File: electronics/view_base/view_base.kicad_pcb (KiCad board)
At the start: 2 copper layers, 81.2 x 81.2 mm, 107 parts, among them J1 BLDC, J2 USB_C_Receptacle_USB2.0, J3 LCD, J4 A, J5 B, Q1 MMBT4403, Q2 UMH3N, U1 MT6701-CT, U2 T-Micro32_Plus, U3 CH340C, U4 HX711, U5 TMC6300, U6 AP2114HA-3.3, U7 SN74LV1T34DBV, U8 VEML7700, U9 TS1117BCW33_RPG

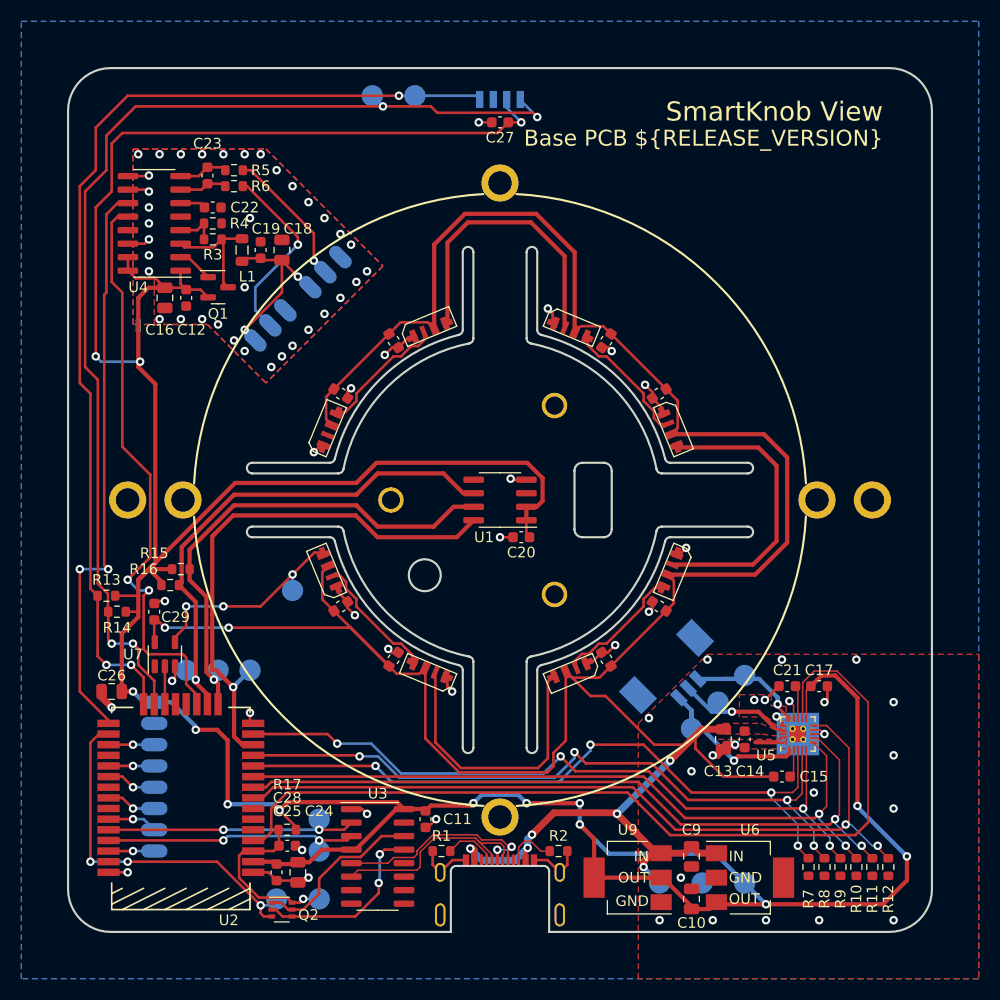
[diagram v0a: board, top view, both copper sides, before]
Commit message: Mod v1
- ESP32-S3-MINI-1N8
- 24x WS2812 20x20 LED
- SMD Resistors 4 direction Force Sensor
- Accelerometer
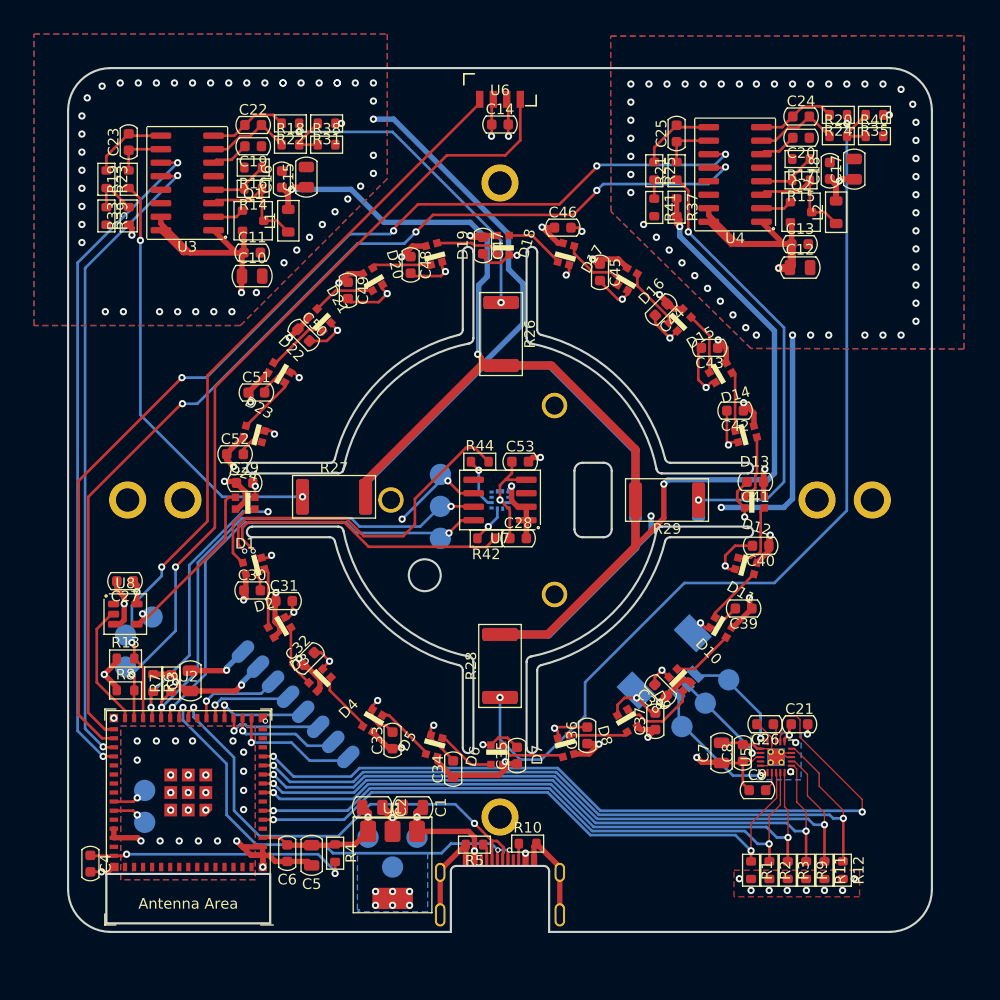
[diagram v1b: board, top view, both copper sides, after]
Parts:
- removed J4: A, SolderPads:SolderPads_2mm_3_STRAIN
- removed J5: B, SolderPads:SolderPads_2mm_3_STRAIN
- removed NT1: NetTie_2, NetTie:NetTie-2_SMD_Pad0.5mm
- removed TP15: TX, Modified:TestPoint_Pad_D2.0mm_ValueSilk
- removed TP16: RX, Modified:TestPoint_Pad_D2.0mm_ValueSilk
- removed U9: TS1117BCW33_RPG, Modified:SOT-223-3_TabPin2_GndOutIn
- removed Z10: BLDCMotor, BOM_Only:bom_only_no_pin
- removed Z7, Z8: RotorScrew (BOM-only), BOM_Only:bom_only_no_pin
- removed Z9: WatchGlass39.5mm, BOM_Only:bom_only_no_pin
- added C30: 0.1uF, Capacitor_SMD_AKL:C_0603_1608Metric, F.Cu at (76.7, 108.5)
- added C31: 0.1uF, Capacitor_SMD_AKL:C_0603_1608Metric, F.Cu at (79.7, 109.5)
- added C32: 0.1uF, Capacitor_SMD_AKL:C_0603_1608Metric, F.Cu at (82.0, 114.9)
- added C33: 0.1uF, Capacitor_SMD_AKL:C_0603_1608Metric, F.Cu at (89.9, 122.6)
- added C34: 0.1uF, Capacitor_SMD_AKL:C_0603_1608Metric, F.Cu at (95.6, 125.3)
- added C35: 0.1uF, Capacitor_SMD_AKL:C_0603_1608Metric, F.Cu at (101.6, 124.0)
- added C36: 0.1uF, Capacitor_SMD_AKL:C_0603_1608Metric, F.Cu at (108.2, 122.1)
- added C37: 0.1uF, Capacitor_SMD_AKL:C_0603_1608Metric, F.Cu at (114.6, 120.8)
- added C38: 0.1uF, Capacitor_SMD_AKL:C_0603_1608Metric, F.Cu at (115.1, 117.9)
- added C39: 0.1uF, Capacitor_SMD_AKL:C_0603_1608Metric, F.Cu at (122.9, 110.2)
- added C40: 0.1uF, Capacitor_SMD_AKL:C_0603_1608Metric, F.Cu at (124.5, 104.3)
- added C41: 0.1uF, Capacitor_SMD_AKL:C_0603_1608Metric, F.Cu at (124.0, 98.3)
- added C42: 0.1uF, Capacitor_SMD_AKL:C_0603_1608Metric, F.Cu at (122.1, 91.6)
- added C43: 0.1uF, Capacitor_SMD_AKL:C_0603_1608Metric, F.Cu at (119.7, 85.7)
- added C44: 0.1uF, Capacitor_SMD_AKL:C_0603_1608Metric, F.Cu at (115.2, 82.1)
- added C45: 0.1uF, Capacitor_SMD_AKL:C_0603_1608Metric, F.Cu at (109.4, 78.6)
- added C46: 0.1uF, Capacitor_SMD_AKL:C_0603_1608Metric, F.Cu at (105.9, 74.4)
- added C47: 0.1uF, Capacitor_SMD_AKL:C_0603_1608Metric, F.Cu at (98.4, 76.1)
- added C48: 0.1uF, Capacitor_SMD_AKL:C_0603_1608Metric, F.Cu at (91.6, 77.9)
- added C49: 0.1uF, Capacitor_SMD_AKL:C_0603_1608Metric, F.Cu at (85.7, 80.3)
- added C50: 0.1uF, Capacitor_SMD_AKL:C_0603_1608Metric, F.Cu at (81.5, 84.5)
- added C51: 0.1uF, Capacitor_SMD_AKL:C_0603_1608Metric, F.Cu at (77.1, 89.9)
- added C52: 0.1uF, Capacitor_SMD_AKL:C_0603_1608Metric, F.Cu at (75.1, 95.7)
- added C53: 1uF, Capacitor_SMD_AKL:C_0603_1608Metric, F.Cu at (101.9, 96.4)
- added D10: WS2812-2020, CrumpPrints:WS2812-2020, F.Cu at (116.9, 116.9)
- added D11: WS2812-2020, CrumpPrints:WS2812-2020, F.Cu at (120.8, 112.0)
- added D12: WS2812-2020, CrumpPrints:WS2812-2020, F.Cu at (123.1, 106.2)
- added D13: WS2812-2020, CrumpPrints:WS2812-2020, F.Cu at (123.9, 100.2)
- added D14: WS2812-2020, CrumpPrints:WS2812-2020, F.Cu at (123.1, 93.8)
- added D15: WS2812-2020, CrumpPrints:WS2812-2020, F.Cu at (120.8, 88.0)
- added D16: WS2812-2020, CrumpPrints:WS2812-2020, F.Cu at (116.9, 83.1)
- added D17: WS2812-2020, CrumpPrints:WS2812-2020, F.Cu at (112.0, 79.2)
- added D18: WS2812-2020, CrumpPrints:WS2812-2020, F.Cu at (106.2, 76.9)
- added D19: WS2812-2020, CrumpPrints:WS2812-2020, F.Cu at (100.3, 76.0)
- added D20: WS2812-2020, CrumpPrints:WS2812-2020, F.Cu at (93.8, 76.9)
- added D21: WS2812-2020, CrumpPrints:WS2812-2020, F.Cu at (88.0, 79.2)
- added D22: WS2812-2020, CrumpPrints:WS2812-2020, F.Cu at (83.1, 83.1)
- added D23: WS2812-2020, CrumpPrints:WS2812-2020, F.Cu at (79.2, 88.0)
- added D24: WS2812-2020, CrumpPrints:WS2812-2020, F.Cu at (76.9, 93.8)
- added D9: WS2812-2020, CrumpPrints:WS2812-2020, F.Cu at (112.0, 120.8)
- added IC1: MXC6655XA, KiCad:MXC6655XA, B.Cu at (100.0, 100.0)
- added L2: 3.3uH, Inductor_SMD_AKL:L_0805_2012Metric, F.Cu at (131.6, 72.9)
- added R18: 100, Resistor_SMD_AKL:R_0603_1608Metric, F.Cu at (80.3, 66.6)
- added R19: 100, Resistor_SMD_AKL:R_0603_1608Metric, F.Cu at (65.1, 69.8)
- added R20: 100, Resistor_SMD_AKL:R_0603_1608Metric, F.Cu at (131.8, 65.8)
- added R21: 100, Resistor_SMD_AKL:R_0603_1608Metric, F.Cu at (116.6, 69.0)
- added R22: 100, Resistor_SMD_AKL:R_0603_1608Metric, F.Cu at (80.3, 64.6)
- added R23: 100, Resistor_SMD_AKL:R_0603_1608Metric, F.Cu at (63.0, 69.8)
- added R24: 100, Resistor_SMD_AKL:R_0603_1608Metric, F.Cu at (131.8, 63.8)
- added R25: 100, Resistor_SMD_AKL:R_0603_1608Metric, F.Cu at (114.5, 69.0)
- added R26: 1K, Resistor_SMD_AKL:R_2512_6332Metric, F.Cu at (100.1, 84.4)
- added R27: 1K, Resistor_SMD_AKL:R_2512_6332Metric, F.Cu at (84.4, 99.7)
- added R28: 1K, Resistor_SMD_AKL:R_2512_6332Metric, F.Cu at (100.0, 115.6)
- added R29: 1K, Resistor_SMD_AKL:R_2512_6332Metric, F.Cu at (115.7, 100.0)
- added R30: 1K, Resistor_SMD_AKL:R_2512_6332Metric, B.Cu at (100.1, 84.4)
- added R31: 1k, Resistor_SMD_AKL:R_0603_1608Metric, F.Cu at (83.7, 64.6)
- added R32: 1K, Resistor_SMD_AKL:R_2512_6332Metric, B.Cu at (84.4, 99.7)
- added R33: 1k, Resistor_SMD_AKL:R_0603_1608Metric, F.Cu at (65.1, 73.3)
- added R34: 1K, Resistor_SMD_AKL:R_2512_6332Metric, B.Cu at (100.0, 115.6)
- added R35: 1k, Resistor_SMD_AKL:R_0603_1608Metric, F.Cu at (135.2, 63.8)
- added R36: 1K, Resistor_SMD_AKL:R_2512_6332Metric, B.Cu at (115.7, 100.3)
- added R37: 1k, Resistor_SMD_AKL:R_0603_1608Metric, F.Cu at (116.6, 72.5)
- added R38: 1k, Resistor_SMD_AKL:R_0603_1608Metric, F.Cu at (83.7, 66.6)
- added R39: 1k, Resistor_SMD_AKL:R_0603_1608Metric, F.Cu at (63.0, 73.3)
- added R40: 1k, Resistor_SMD_AKL:R_0603_1608Metric, F.Cu at (135.2, 65.8)
- added R41: 1k, Resistor_SMD_AKL:R_0603_1608Metric, F.Cu at (114.5, 72.5)
- added R42: 2.7k, Resistor_SMD_AKL:R_0603_1608Metric, F.Cu at (98.7, 103.6)
- added R44: 2.7k, Resistor_SMD_AKL:R_0603_1608Metric, F.Cu at (98.1, 96.4)
- C1, C12, C15, C17, C2, C3, C5: value 0.1uF -> 10uF; footprint Capacitor_SMD:C_0603_1608Metric -> Capacitor_SMD_AKL:C_0805_2012Metric
- C10: footprint Capacitor_SMD:C_0805_2012Metric -> Capacitor_SMD_AKL:C_0805_2012Metric
- C11, C14, C19, C20, C21, C22, C23, C25, C27, C29, C6, C8: footprint Capacitor_SMD:C_0603_1608Metric -> Capacitor_SMD_AKL:C_0603_1608Metric
- C13: value 22uF -> 0.1uF; footprint Capacitor_SMD:C_0805_2012Metric -> Capacitor_SMD_AKL:C_0603_1608Metric
- C16, C18, C24, C26, C9: value 10uF -> 0.1uF; footprint Capacitor_SMD:C_0805_2012Metric -> Capacitor_SMD_AKL:C_0603_1608Metric
- C28: value 1uF -> 0.1uF; footprint Capacitor_SMD:C_0603_1608Metric -> Capacitor_SMD_AKL:C_0603_1608Metric
- C4: value 0.1uF -> 1uF; footprint Capacitor_SMD:C_0603_1608Metric -> Capacitor_SMD_AKL:C_0603_1608Metric
- C7: value 0.1uF -> 22uF; footprint Capacitor_SMD:C_0603_1608Metric -> Capacitor_SMD_AKL:C_0805_2012Metric
- D1, D2, D3, D4, D5, D6, D7, D8: value SK6812SIDE-A -> WS2812-2020; footprint sk6812:SK6812-SIDE-A -> CrumpPrints:WS2812-2020
- J1: value BLDC -> LCD; footprint Molex:532610371 -> SolderPads:SolderPads_2mm_8
- J3: value LCD -> BLDC; footprint SolderPads:SolderPads_2mm_8 -> Molex:532610371
- L1: footprint Inductor_SMD:L_0805_2012Metric -> Inductor_SMD_AKL:L_0805_2012Metric
- Q1: footprint Package_TO_SOT_SMD:SOT-23 -> Package_TO_SOT_SMD_AKL:SOT-23
- Q2: value UMH3N -> MMBT4403; footprint Package_TO_SOT_SMD:SOT-363_SC-70-6 -> Package_TO_SOT_SMD_AKL:SOT-23
- R1, R2: value 5.1k -> 10k; footprint Resistor_SMD:R_0603_1608Metric -> Resistor_SMD_AKL:R_0603_1608Metric
- R10: value 10k -> 5.1k; footprint Resistor_SMD:R_0603_1608Metric -> Resistor_SMD_AKL:R_0603_1608Metric
- R11, R12, R13, R3, R9: footprint Resistor_SMD:R_0603_1608Metric -> Resistor_SMD_AKL:R_0603_1608Metric
- R14, R15: value 2.2k -> 10k; footprint Resistor_SMD:R_0603_1608Metric -> Resistor_SMD_AKL:R_0603_1608Metric
- R16: value 2.2k -> 8.2k; footprint Resistor_SMD:R_0603_1608Metric -> Resistor_SMD_AKL:R_0603_1608Metric
- R17: value 10k -> 8.2k; footprint Resistor_SMD:R_0603_1608Metric -> Resistor_SMD_AKL:R_0603_1608Metric
- R4: value 8.2k -> 10k; footprint Resistor_SMD:R_0603_1608Metric -> Resistor_SMD_AKL:R_0603_1608Metric
- R5: value 100 -> 5.1k; footprint Resistor_SMD:R_0603_1608Metric -> Resistor_SMD_AKL:R_0603_1608Metric
- R6: value 100 -> 2.2k; footprint Resistor_SMD:R_0603_1608Metric -> Resistor_SMD_AKL:R_0603_1608Metric
- R7, R8: value 10k -> 2.2k; footprint Resistor_SMD:R_0603_1608Metric -> Resistor_SMD_AKL:R_0603_1608Metric
- TP10: value CLK -> W
- TP11: value DO -> LED
- TP12: value LED -> CSN
- TP13: value EN -> CLK
- TP14: value BOOT -> DO
- TP3: value GND -> TX
- TP4: value SDA -> RX
- TP5: value SCL -> GND
- TP6: value U -> SDA
- TP7: value V -> SCL
- TP8: value W -> U
- TP9: value CSN -> V
- U1: value MT6701-CT -> AP2114HA-3.3; footprint Package_SO:SOIC-8_3.9x4.9mm_P1.27mm -> Package_TO_SOT_SMD_AKL:SOT-223-3_TabPin2
- U2: value T-Micro32_Plus -> ESP32-S3-MINI-1; footprint lilygo_micro32:T-Micro32 -> Espressif:ESP32-S3-MINI-1
- U3: value CH340C -> HX711; footprint Package_SO:SOIC-16_3.9x9.9mm_P1.27mm -> Package_SO_AKL:SOIC-16_3.9x9.9mm_P1.27mm
- U4: footprint Package_SO:SOIC-16_3.9x9.9mm_P1.27mm -> Package_SO_AKL:SOIC-16_3.9x9.9mm_P1.27mm
- U6: value AP2114HA-3.3 -> VEML7700; footprint Modified:SOT-223-3_TabPin2_InGndOut -> VEML7700:VEML7700-TOP
- U7: value SN74LV1T34DBV -> MT6701-CT; footprint Package_TO_SOT_SMD:SOT-23-5 -> Package_SO_AKL:SOIC-8_3.9x4.9mm_P1.27mm
- U8: value VEML7700 -> SN74LV1T34DBV; footprint VEML7700:VEML7700-TOP -> Package_TO_SOT_SMD_AKL:SOT-23-5; moved to F.Cu
- Z1, Z2, Z3: value BF350-3AA Strain Gauge -> RotorScrew (BOM-only); footprint strain:BF350-3AA -> BOM_Only:bom_only_no_pin; moved to F.Cu
- Z4: value BF350-3AA Strain Gauge -> WatchGlass39.5mm; footprint strain:BF350-3AA -> BOM_Only:bom_only_no_pin; moved to F.Cu
- Z5: value dummy_keepouts -> BLDCMotor; footprint view_custom:ViewKeepouts3d -> BOM_Only:bom_only_no_pin
- Z6: value RotorScrew (BOM-only) -> dummy_keepouts; footprint BOM_Only:bom_only_no_pin -> view_custom:ViewKeepouts3d
- moved Z4 105.9 mm to (177.0, 65.7), turned to 0 degrees
- moved Z3 96.7 mm to (177.4, 73.4), turned to 0 degrees
- moved C24 85.4 mm to (128.3, 63.9), turned to 0 degrees
- moved Z5 83.5 mm to (177.2, 68.1)
- moved Q2 81.7 mm to (128.3, 72.9)
- moved R3 80.2 mm to (127.0, 134.8), turned to -90 degrees
- moved R17 79.4 mm to (128.3, 68.0)
- moved C25 79.0 mm to (116.6, 65.5), turned to 90 degrees
- moved U6 78.1 mm to (100.0, 61.0)
- moved TP4 72.9 mm to (66.6, 130.3), turned to 180 degrees
- moved TP5 72.5 mm to (89.9, 134.5), turned to 90 degrees
- moved C15 71.9 mm to (81.8, 69.6), turned to 90 degrees
- moved C10 71.7 mm to (76.7, 78.9), turned to 0 degrees
- moved R15 70.5 mm to (128.3, 69.9), turned to 180 degrees
- moved Z1 68.1 mm to (177.1, 70.8), turned to 0 degrees
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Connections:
- C12 pad 2: GNDA -> GND
- C13 pad 1: +5V -> +3V3
- C14 pad 1: +5V -> +3V3
- C15 pad 1: +5V -> /AVDD
- C15 pad 2: Net-(C15-Pad2) -> GND
- C16 pad 1: +3V3 -> /AVDD
- C16 pad 2: GNDA -> GND
- C17 pad 1: +3V3 -> /AVDD
- C18 pad 1: /STRAIN_E+ -> /AVDD
- C18 pad 2: GNDA -> GND
- C19 pad 1: /STRAIN_E+ -> GND
- C19 pad 2: GNDA -> Net-(C19-Pad2)
- C2 pad 1: +5V -> +3V3
- C20 pad 1: +3V3 -> GND
- C20 pad 2: GND -> Net-(C20-Pad2)
- C21 pad 1: Net-(C21-Pad1) -> +3V3
- C22 pad 1: GNDA -> Net-(C22-Pad1)
- C24 pad 1: +3V3 -> Net-(C24-Pad1)
- C24 pad 2: GND -> Net-(C24-Pad2)
- C25 pad 1: +3V3 -> Net-(C25-Pad1)
- C25 pad 2: GND -> Net-(C25-Pad2)
- C26 pad 1: +3V3 -> Net-(C26-Pad1)
- C27 pad 1: +3V3 -> +5V
- C28 pad 1: /ESP32_EN -> GND
- C28 pad 2: GND -> +3V3
- C3 pad 1: +5V -> +3V3
- C4 pad 1: +5V -> /ESP32_EN
- C5 pad 1: +5V -> +3V3
- C6 pad 1: +5V -> +3V3
- C9 pad 2: GND -> Net-(C9-Pad2)
- D1 pad 1: /LED_DATA_5V -> Net-(D1-Pad1)
- D1 pad 2: +5V -> GND
- D1 pad 3: Net-(D1-Pad3) -> /LED_DATA_5V
- D1 pad 4: GND -> +5V
- D2 pad 1: Net-(D1-Pad3) -> Net-(D2-Pad1)
- D2 pad 2: +5V -> GND
- D2 pad 3: Net-(D2-Pad3) -> Net-(D1-Pad1)
- D2 pad 4: GND -> +5V
- D3 pad 1: Net-(D2-Pad3) -> Net-(D3-Pad1)
- D3 pad 2: +5V -> GND
- D3 pad 3: Net-(D3-Pad3) -> Net-(D2-Pad1)
- D3 pad 4: GND -> +5V
- D4 pad 1: Net-(D3-Pad3) -> Net-(D4-Pad1)
- D4 pad 2: +5V -> GND
- D4 pad 3: Net-(D4-Pad3) -> Net-(D3-Pad1)
- D4 pad 4: GND -> +5V
- D5 pad 1: Net-(D4-Pad3) -> Net-(D5-Pad1)
- D5 pad 2: +5V -> GND
- D5 pad 3: Net-(D5-Pad3) -> Net-(D4-Pad1)
- D5 pad 4: GND -> +5V
- D6 pad 1: Net-(D5-Pad3) -> Net-(D6-Pad1)
- D6 pad 2: +5V -> GND
- D6 pad 3: Net-(D6-Pad3) -> Net-(D5-Pad1)
- D6 pad 4: GND -> +5V
- D7 pad 1: Net-(D6-Pad3) -> Net-(D7-Pad1)
- D7 pad 2: +5V -> GND
- D7 pad 3: Net-(D7-Pad3) -> Net-(D6-Pad1)
- D7 pad 4: GND -> +5V
- D8 pad 1: Net-(D7-Pad3) -> Net-(D8-Pad1)
- D8 pad 2: +5V -> GND
- D8 pad 3: unconnected-(D8-Pad3) -> Net-(D7-Pad1)
- D8 pad 4: GND -> +5V
- J1 pad 1: Net-(J1-Pad1) -> GND
- J1 pad 2: Net-(J1-Pad2) -> +3V3
- J1 pad 3: Net-(J1-Pad3) -> /LCD_BL
- J3 pad 1: +3V3 -> Net-(J3-Pad1)
- J3 pad 2: GND -> Net-(J3-Pad2)
- J3 pad 3: /LCD_RST -> Net-(J3-Pad3)
- L1 pad 2: /STRAIN_E+ -> /AVDD
- Q2 pad 1: /RTS -> Net-(Q2-Pad1)
- Q2 pad 2: /DTR -> +3V3
- Q2 pad 3: /ESP32_BOOT -> Net-(L2-Pad1)
- R1 pad 1: /USB_CC1 -> /TMC_UH
- R10 pad 1: /TMC_UL -> /USB_CC2
- R13 pad 2: /SDA -> /SCL
- R14 pad 1: +3V3 -> Net-(L1-Pad1)
- R14 pad 2: /SCL -> Net-(R14-Pad2)
- R15 pad 1: +3V3 -> Net-(L2-Pad1)
- R15 pad 2: /MAG_DO -> Net-(R15-Pad2)
- R16 pad 1: /MAG_CLK -> Net-(R14-Pad2)
- R16 pad 2: +3V3 -> GND
- R17 pad 1: +3V3 -> Net-(R15-Pad2)
- R17 pad 2: /ESP32_EN -> GND
- R2 pad 1: /USB_CC2 -> /TMC_VH
- R3 pad 1: Net-(L1-Pad1) -> /TMC_WH
- R3 pad 2: Net-(R3-Pad2) -> GND
- R4 pad 1: Net-(R3-Pad2) -> +3V3
- R4 pad 2: GNDA -> /ESP32_EN
- R5 pad 1: Net-(C23-Pad2) -> /USB_CC1
- R5 pad 2: /STRAIN_S- -> GND
- R6 pad 1: /STRAIN_S+ -> +3V3
- R6 pad 2: Net-(C23-Pad1) -> /MAG_DO
- R7 pad 1: /TMC_UH -> /MAG_CLK
- R7 pad 2: GND -> +3V3
- R8 pad 1: /TMC_VH -> +3V3
- R8 pad 2: GND -> /SDA
- R9 pad 1: /TMC_WH -> /TMC_UL
- TP10 pad 1: /MAG_CLK -> Net-(J3-Pad1)
- TP11 pad 1: /MAG_DO -> /LED_DATA_5V
- TP12 pad 1: /LED_DATA_5V -> /MAG_CSN
- TP13 pad 1: /ESP32_EN -> /MAG_CLK
- TP14 pad 1: /ESP32_BOOT -> /MAG_DO
- TP3 pad 1: GND -> Net-(TP3-Pad1)
- TP4 pad 1: /SDA -> Net-(TP4-Pad1)
- TP5 pad 1: /SCL -> GND
- TP6 pad 1: Net-(J1-Pad3) -> /SDA
- TP7 pad 1: Net-(J1-Pad2) -> /SCL
- TP8 pad 1: Net-(J1-Pad1) -> Net-(J3-Pad3)
- TP9 pad 1: /MAG_CSN -> Net-(J3-Pad2)
- U1 pad 1: +3V3 -> +5V
- U1 pad 2: +3V3 -> GND
- U1 pad 3: unconnected-(U1-Pad3) -> +3V3
- U2 pad 10: /TMC_UL -> /TMC_WL
- U2 pad 11: /TMC_UH -> /TMC_VL
- U2 pad 12: /TMC_VH -> /TMC_DIAG
- U2 pad 13: /MAG_CSN -> unconnected-(U2-Pad13)
- U2 pad 14: /TMC_WH -> unconnected-(U2-Pad14)
- U2 pad 15: GND -> unconnected-(U2-Pad15)
- U2 pad 16: /MAG_CLK -> /LCD_RST
- U2 pad 17: /MAG_DO -> /LCD_DATA
- U2 pad 18: /STRAIN_DO -> /LCD_SCK
- U2 pad 19: unconnected-(U2-Pad19) -> /LCD_CS
- U2 pad 2: +3V3 -> GND
- U2 pad 20: unconnected-(U2-Pad20) -> /LCD_CMD
- U2 pad 21: /LED_DATA_3V3 -> /LCD_BL
- U2 pad 22: /SCL -> unconnected-(U2-Pad22)
- U2 pad 23: /SDA -> /USB_D-
- U2 pad 24: /STRAIN_SCK -> /USB_D+
- U2 pad 25: /ESP32_BOOT -> /MAG_CSN
- U2 pad 26: /LCD_RST -> /MAG_CLK
- U2 pad 27: unconnected-(U2-Pad27) -> /MAG_DO
- U2 pad 28: /LCD_SCK -> /SCL
- U2 pad 29: /LCD_DATA -> /SDA
- U2 pad 3: /ESP32_EN -> +3V3
- U2 pad 30: unconnected-(U2-Pad30) -> /LED_DATA
- U2 pad 31: /LCD_BACKLIGHT -> /STRAIN2_DO
- U2 pad 32: unconnected-(U2-Pad32) -> /STRAIN2_SCK
- U2 pad 33: /LCD_CS -> /STRAIN1_DO
- U2 pad 34: /USB_SERIAL_TXO -> /STRAIN1_SCK
- U2 pad 35: /USB_SERIAL_RXI -> unconnected-(U2-Pad35)
- U2 pad 36: /LCD_CMD -> unconnected-(U2-Pad36)
- U2 pad 38: GND -> unconnected-(U2-Pad38)
- U2 pad 4: /TMC_DIAG -> unconnected-(U2-Pad4)
- U2 pad 5: unconnected-(U2-Pad5) -> /TMC_UH
- U2 pad 6: unconnected-(U2-Pad6) -> /TMC_VH
- U2 pad 8: /TMC_VL -> /TMC_WH
- U2 pad 9: /TMC_WL -> /TMC_UL
- U3 pad 1: GND -> +3V3
- U3 pad 10: unconnected-(U3-Pad10) -> Net-(C23-Pad1)
- U3 pad 11: unconnected-(U3-Pad11) -> /STRAIN1_SCK
- U3 pad 12: unconnected-(U3-Pad12) -> /STRAIN1_DO
- U3 pad 13: /DTR -> unconnected-(U3-Pad13)
- U3 pad 14: /RTS -> GND
- U3 pad 15: unconnected-(U3-Pad15) -> +3V3
- U3 pad 2: /USB_SERIAL_TXO -> Net-(Q1-Pad1)
- U3 pad 3: /USB_SERIAL_RXI -> Net-(L1-Pad1)
- U3 pad 4: +3V3 -> Net-(R14-Pad2)
- U3 pad 5: /USB_D+ -> GND
- U3 pad 6: /USB_D- -> Net-(C19-Pad2)
- U3 pad 7: unconnected-(U3-Pad7) -> Net-(C22-Pad2)
- U3 pad 8: unconnected-(U3-Pad8) -> Net-(C22-Pad1)
- U3 pad 9: unconnected-(U3-Pad9) -> Net-(C23-Pad2)
- U4 pad 10: GNDA -> Net-(C25-Pad1)
- U4 pad 11: /STRAIN_SCK -> /STRAIN2_SCK
- U4 pad 12: /STRAIN_DO -> /STRAIN2_DO
- U4 pad 14: GNDA -> GND
- U4 pad 2: Net-(Q1-Pad1) -> Net-(Q2-Pad1)
- U4 pad 3: Net-(L1-Pad1) -> Net-(L2-Pad1)
- U4 pad 4: Net-(R3-Pad2) -> Net-(R15-Pad2)
- U4 pad 5: GNDA -> GND
- U4 pad 6: Net-(C22-Pad2) -> Net-(C20-Pad2)
- U4 pad 7: Net-(C23-Pad2) -> Net-(C24-Pad2)
- U4 pad 8: Net-(C23-Pad1) -> Net-(C24-Pad1)
- U4 pad 9: GNDA -> Net-(C25-Pad2)
- U5 pad 1: Net-(J1-Pad1) -> Net-(J3-Pad1)
- U5 pad 13: Net-(C21-Pad1) -> Net-(C26-Pad1)
- U5 pad 15: Net-(J1-Pad3) -> Net-(J3-Pad3)
- U5 pad 17: Net-(J1-Pad2) -> Net-(J3-Pad2)
- U5 pad 2: Net-(C15-Pad2) -> Net-(C9-Pad2)
- U6 pad 1: +5V -> /SCL
- U6 pad 2: GND -> +3V3
- U6 pad 3: +3V3 -> GND
- U7 pad 1: unconnected-(U7-Pad1) -> +3V3
- U7 pad 2: /LED_DATA_3V3 -> +3V3
- U7 pad 3: GND -> unconnected-(U7-Pad3)
- U7 pad 4: /LED_DATA_5V -> GND
- U7 pad 5: +5V -> unconnected-(U7-Pad5)
- U8 pad 1: /SCL -> unconnected-(U8-Pad1)
- U8 pad 2: +3V3 -> /LED_DATA
- U8 pad 4: /SDA -> /LED_DATA_5V
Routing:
- net GND: track 69.1 -> 300.2 mm, vias 47 -> 175
- net /AVDD: track 0.00 -> 213.2 mm, vias 0 -> 8
- net +5V: track 256.1 -> 459.7 mm, vias 8 -> 28
- net /STRAIN2_SCK: track 0.00 -> 101.5 mm, vias 0 -> 4
- net /STRAIN2_DO: track 0.00 -> 97.7 mm, vias 0 -> 4
- net /IN2A+: track 0.00 -> 86.1 mm, vias 0 -> 2
- net /STRAIN1_SCK: track 0.00 -> 63.3 mm, vias 0 -> 2
- net /STRAIN1_DO: track 0.00 -> 60.6 mm, vias 0 -> 2
- net /STRAIN_DO: track 55.3 -> 0.00 mm, vias 2 -> 0
- net /STRAIN_SCK: track 54.5 -> 0.00 mm, vias 2 -> 0
- net /IN2B+: track 0.00 -> 41.3 mm, vias 0 -> 2
- net /IN1B+: track 0.00 -> 40.2 mm, vias 0 -> 2
- net /ESP32_BOOT: track 34.9 -> 0.00 mm, vias 3 -> 0
- net /IN1A+: track 0.00 -> 29.9 mm, vias 0 -> 2
- net /SDA: track 97.0 -> 125.1 mm
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- added copper zone on In1.Cu, net GND
- added copper zone on In2.Cu, net GND
- removed copper zone on F.Cu, net +5V
- removed copper zone on B.Cu, net GNDA
- removed copper zone on F.Cu, net GNDA
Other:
- outline, holes or cut-outs redrawn
- copper layers 2 -> 4
- board text removed: "+"
- board text removed: "-"
- board text removed: "A"
- board text removed: "B"
- board text removed: "Base PCB ${RELEASE_VERSION}"
- board text removed: "C"
- board text removed: "D"
- board text removed: "DATE: ${COMMIT_DATE_LONG} COMMIT: ${COMMIT_HASH}"
- board text removed: "Display"
- board text removed: "M"
- board text removed: "Motor"
- board text removed: "R"
- board text removed: "S"
- board text removed: "SmartKnob View"
- board text removed: "Strain"
